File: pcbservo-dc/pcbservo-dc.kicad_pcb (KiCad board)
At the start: 4 copper layers, 58 x 66 mm, 86 parts, among them IC1 NC7WZ241K8X, IC2 NC7WZ241K8X, IC3 NC7WZ241K8X, J1 Conn_01x02, J10 Conn_01x03, J12 Conn_01x02, J13 Conn_01x02, J14 R-78B5.0-2.0, J2 Conn_01x02, J3 BU33SD5WG-TR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

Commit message: uart a jour
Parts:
- removed H3: MountingHole_Pad, MountingHole:MountingHole_2.7mm_M2.5_Pad
- removed J8: Conn_01x03, Connector_JST:JST_PH_B3B-PH-K_1x03_P2.00mm_Vertical
- removed R16: 220, Resistor_SMD:R_0402_1005Metric
- added J6: Conn_01x05, Connector_JST:JST_XH_B5B-XH-A_1x05_P2.50mm_Vertical, F.Cu at (168.5, 85.2)
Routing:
- net +3.3V: track 76.2 -> 83.3 mm, vias 8 -> 9
- net USART1_RX: track 33.1 -> 38.1 mm
- net Net-(J8-Pin_2): track 4.40 -> 0.00 mm
- net Net-(J6-Pin_5): track 4.39 -> 7.42 mm
- net GND: vias 79 -> 78

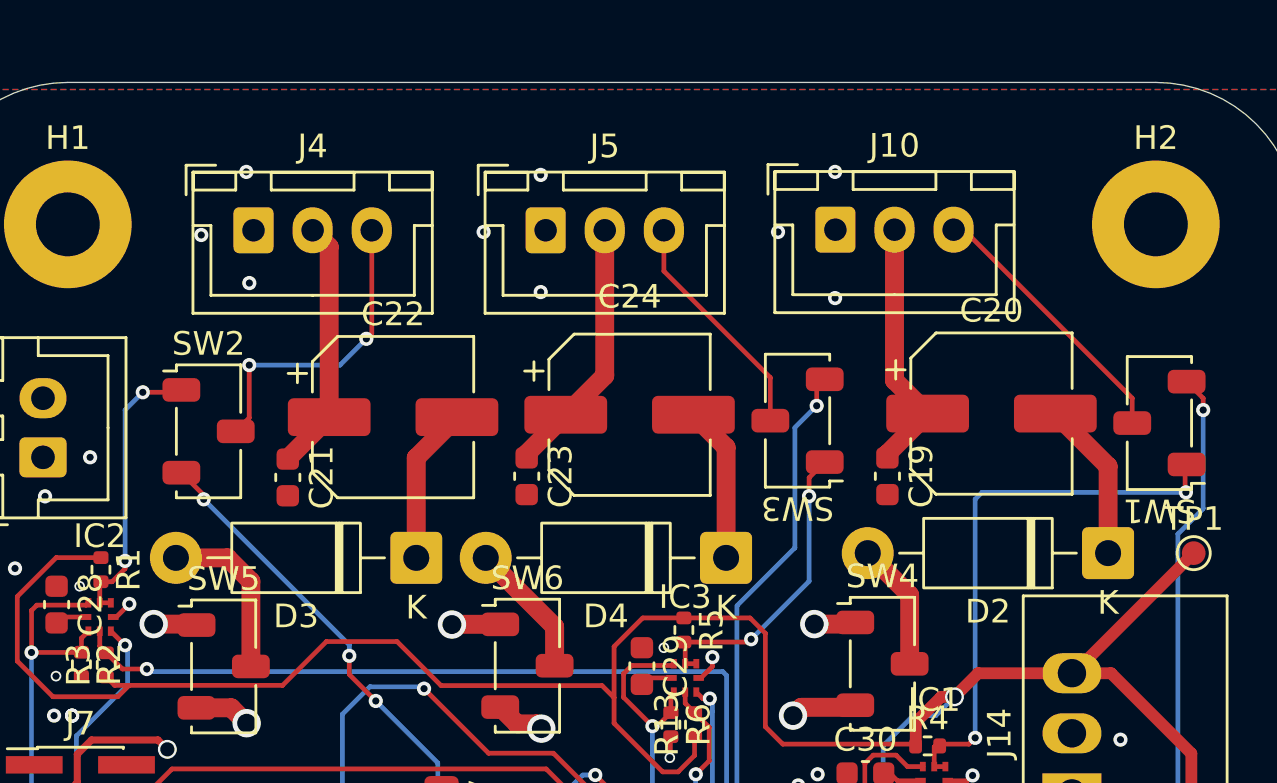
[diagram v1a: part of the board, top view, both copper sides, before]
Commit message: modification des condensateur et des diode
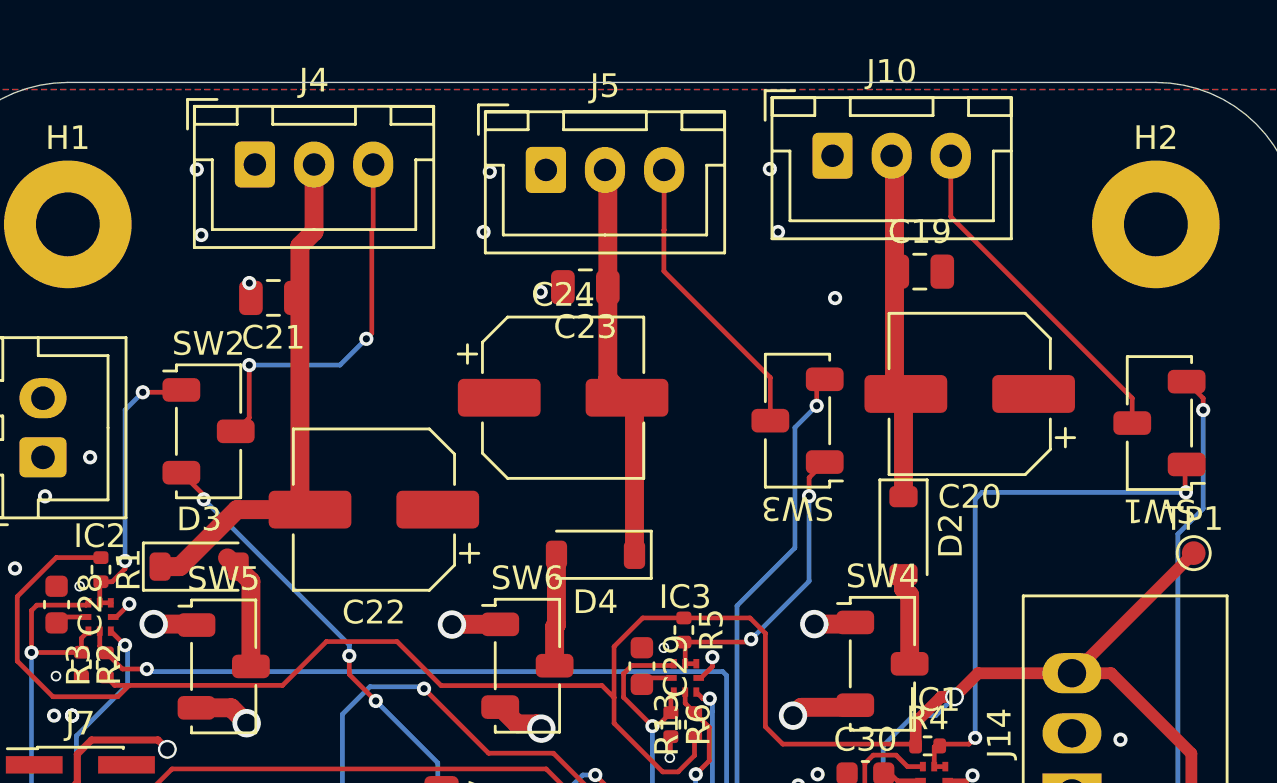
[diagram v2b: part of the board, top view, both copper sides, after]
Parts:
- C19: value 100n -> 47µ; footprint Capacitor_SMD:C_0603_1608Metric -> Capacitor_SMD:C_0805_2012Metric
- C20, C22, C24: value 47µ -> 220µ; footprint Capacitor_SMD:CP_Elec_6.3x5.7 -> Capacitor_SMD:CP_Elec_6.3x5.8
- C21, C23: value 0.1µ -> 47µ; footprint Capacitor_SMD:C_0603_1608Metric -> Capacitor_SMD:C_0805_2012Metric
- D2, D3, D4: footprint Diode_THT:D_DO-41_SOD81_P10.16mm_Horizontal -> Diode_SMD:D_SOD-123
- R15: value 220 -> 51
- moved D3 9.18 mm to (175.6, 58.5), turned to 0 degrees
- moved C19 8.76 mm to (206.0, 46.0), turned to 0 degrees
- moved D2 8.68 mm to (205.3, 57.2), turned to -90 degrees
- moved C23 8.37 mm to (191.9, 46.7), turned to 180 degrees
- moved C21 7.61 mm to (178.7, 47.1), turned to 180 degrees
- moved D4 5.52 mm to (192.3, 58.0)
- moved C22 3.99 mm to (182.9, 56.1), turned to 180 degrees
- moved J10 3.13 mm to (202.3, 41.1)
- moved C24 2.90 mm to (190.9, 51.3)
- moved J4 2.78 mm to (177.9, 41.5)
- moved J5 2.55 mm to (190.2, 41.7)
- moved C20 1.24 mm to (208.1, 51.2), turned to 180 degrees
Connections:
- C19 pad 1: Net-(J10-Pin_2) -> Net-(D2-K)
- C20 pad 1: Net-(J10-Pin_2) -> GND
- C21 pad 1: Net-(J4-Pin_2) -> Net-(D3-K)
- C22 pad 1: Net-(J4-Pin_2) -> GND
- C23 pad 1: Net-(J5-Pin_2) -> Net-(D4-K)
- C24 pad 1: Net-(J5-Pin_2) -> GND
- J10 pad 2: Net-(J10-Pin_2) -> Net-(D2-K)
- J4 pad 2: Net-(J4-Pin_2) -> Net-(D3-K)
- J5 pad 2: Net-(J5-Pin_2) -> Net-(D4-K)
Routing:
- net Net-(D3-K): track 6.66 -> 22.4 mm
- net Net-(J5-Pin_2): track 11.0 -> 0.00 mm
- net Net-(J10-Pin_2): track 10.9 -> 0.00 mm
- net Net-(J4-Pin_2): track 10.7 -> 0.00 mm
- net Net-(D4-K): track 6.62 -> 16.8 mm
- net Net-(D2-K): track 6.82 -> 13.9 mm
- net PWM_UART1: track 11.6 -> 14.5 mm
- net PWM_UART2: track 13.1 -> 15.9 mm
- net PWM_UART3: track 9.91 -> 12.5 mm
- net Alim_servo2: track 7.18 -> 5.00 mm
- net Alim_servo1: track 5.41 -> 3.88 mm
- net Alim_servo3: track 5.77 -> 4.72 mm

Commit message: changement de quelques empreinte
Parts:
- C19: value 47µ -> 0µ1
- C20, C22, C24: footprint Capacitor_SMD:CP_Elec_6.3x5.8 -> EEUFS1K221LB:CAPPRD500W60D1000H2500
- C21, C23: value 47µ -> 0.1µ
- J1, J12, J13, J2: footprint Connector_JST:JST_XH_B2B-XH-A_1x02_P2.50mm_Vertical -> Connector_JST:JST_EH_B2B-EH-A_1x02_P2.50mm_Vertical
- J10, J4, J5: footprint Connector_JST:JST_XH_B3B-XH-A_1x03_P2.50mm_Vertical -> Connector_JST:JST_EH_B3B-EH-A_1x03_P2.50mm_Vertical
- J6: footprint Connector_JST:JST_XH_B5B-XH-A_1x05_P2.50mm_Vertical -> Connector_JST:JST_EH_B5B-EH-A_1x05_P2.50mm_Vertical
- moved C19 2.39 mm to (203.9, 44.9), turned to 180 degrees
- moved C23 2.12 mm to (191.9, 44.5)
- moved SW1 1.54 mm to (217.7, 52.3)
- moved C20 1.49 mm to (209.3, 50.3), turned to 0 degrees
- moved C24 1.35 mm to (192.3, 51.1), turned to 180 degrees
- moved J5 0.89 mm to (190.2, 40.8)
- moved C21 0.82 mm to (179.5, 47.1)
- moved SW2 0.58 mm to (175.4, 52.7)
- moved C22 0.35 mm to (182.8, 55.7), turned to 0 degrees
- moved D3 0.25 mm to (175.3, 58.5)
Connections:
- C20 pad 1: GND -> Net-(D2-K)
- C20 pad 2: Net-(D2-K) -> GND
- C22 pad 1: GND -> Net-(D3-K)
- C22 pad 2: Net-(D3-K) -> GND
- C24 pad 1: GND -> Net-(D4-K)
- C24 pad 2: Net-(D4-K) -> GND
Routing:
- net Net-(D2-K): track 13.9 -> 16.4 mm
- net Net-(D4-K): track 16.8 -> 18.4 mm
- net DXL_PWR1: track 23.6 -> 24.8 mm
- net PWM_UART1: track 14.5 -> 15.6 mm
